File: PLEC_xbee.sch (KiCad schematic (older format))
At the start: 3 parts, among them IC1 XBP9B-DMST-002

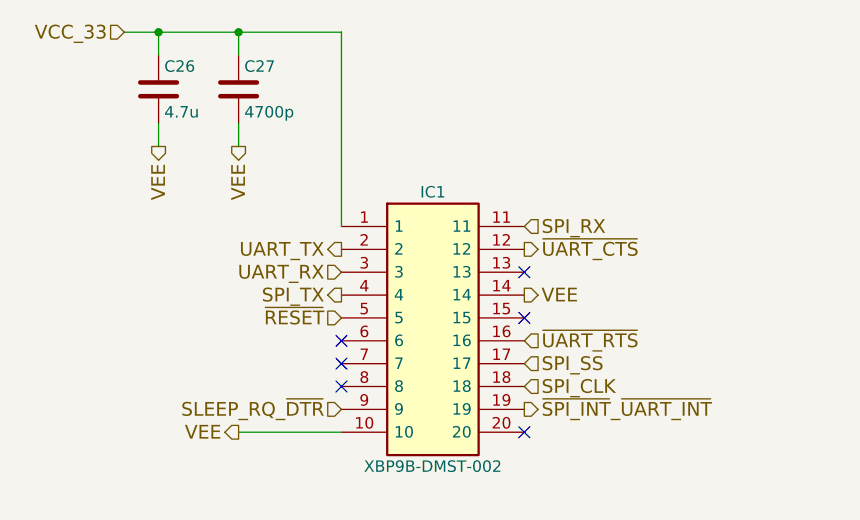
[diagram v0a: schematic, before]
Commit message: Almost done with layout; need to rearrange uC pins
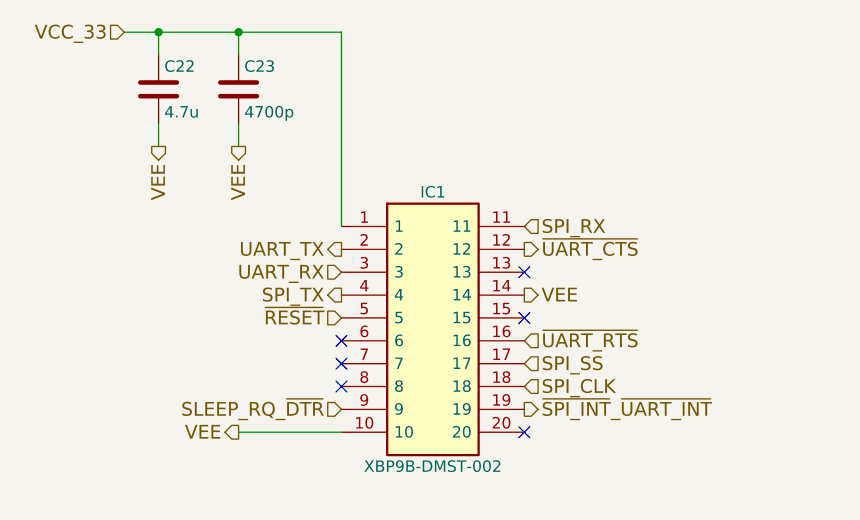
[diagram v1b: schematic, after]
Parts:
- renumbered C26 to C22, C27 to C23
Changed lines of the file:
@@
 NoConn ~ 4850 3800
 $Comp
-L C C27
+L C C23
 U 1 1 5A71C0C2
 P 4400 2500
-F 0 "C27" H 4425 2600 50  0000 L CNN
+F 0 "C23" H 4425 2600 50  0000 L CNN
 F 1 "4700p" H 4425 2400 50  0000 L CNN
 F 2 "PLEC:THTt_100Px150Lx100Wx183H_4700p" H 4438 2350 50  0001 C CNN
@@
 	4400 2750 4400 2650
 $Comp
-L C C26
+L C C22
 U 1 1 5A76736C
 P 4050 2500
-F 0 "C26" H 4075 2600 50  0000 L CNN
+F 0 "C22" H 4075 2600 50  0000 L CNN
 F 1 "4.7u" H 4075 2400 50  0000 L CNN
 F 2 "PLEC:THTm_1.5Px4Dx7H_4.7u" H 4088 2350 50  0001 C CNN

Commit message: Replaced solid state relays with NPN Darlingtons
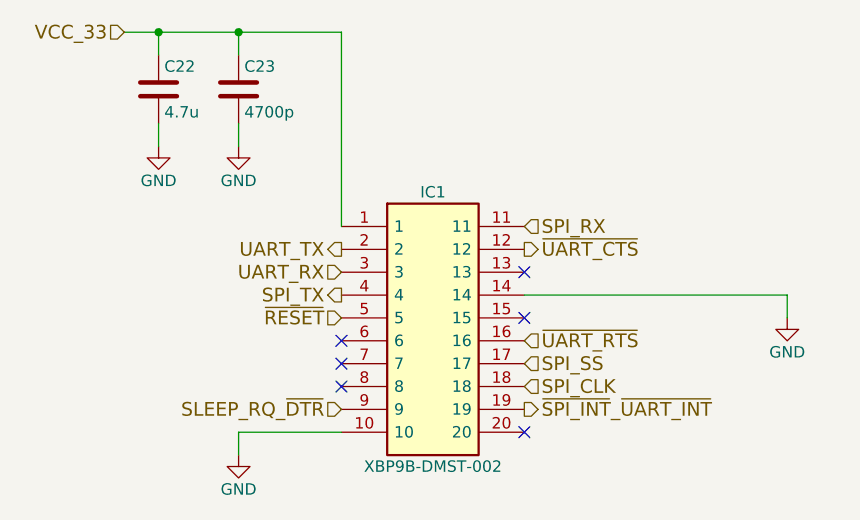
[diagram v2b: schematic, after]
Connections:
- net VEE renamed GND
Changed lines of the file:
@@
 EESchema Schematic File Version 2
+LIBS:PLEC-rescue
 LIBS:power
 LIBS:device
@@
 LIBS:PLEC
 LIBS:cap_470u
+LIBS:BDW42G
 LIBS:PLEC-cache
 EELAYER 25 0
@@
 $Descr A4 11693 8268
 encoding utf-8
-Sheet 7 9
+Sheet 6 9
 Title ""
 Date ""
@@
 NoConn ~ 4850 3700
 NoConn ~ 4850 3600
-Text HLabel 4400 4000 0    60   Output ~ 0
-VEE
-Text HLabel 5650 3400 2    60   Output ~ 0
-VEE
-Text HLabel 4400 2750 3    60   Output ~ 0
-VEE
 Wire Wire Line
 	4400 2350 4400 2250
@@
 	1    0    0    -1
 $EndComp
-Text HLabel 4050 2750 3    60   Output ~ 0
-VEE
 Wire Wire Line
 	4050 2750 4050 2650
@@
 	4050 2350 4050 2250
 Connection ~ 4050 2250
+Wire Wire Line
+	4400 4100 4400 4000
+$Comp
+L GND #PWR028
+U 1 1 5A8488B5
+P 4400 4100
+F 0 "#PWR028" H 4400 3850 50  0001 C CNN
+F 1 "GND" H 4400 3950 50  0000 C CNN
+F 2 "" H 4400 4100 50  0001 C CNN
+F 3 "" H 4400 4100 50  0001 C CNN
+	1    4400 4100
+	1    0    0    -1
+$EndComp
+Wire Wire Line
+	5650 3400 6800 3400
+Wire Wire Line
+	6800 3400 6800 3500
+$Comp
+L GND #PWR029
+U 1 1 5A848C7E
+P 6800 3500
+F 0 "#PWR029" H 6800 3250 50  0001 C CNN
+F 1 "GND" H 6800 3350 50  0000 C CNN
+F 2 "" H 6800 3500 50  0001 C CNN
+F 3 "" H 6800 3500 50  0001 C CNN
+	1    6800 3500
+	1    0    0    -1
+$EndComp
+$Comp
+L GND #PWR030
+U 1 1 5A8494C9
+P 4050 2750
+F 0 "#PWR030" H 4050 2500 50  0001 C CNN
+F 1 "GND" H 4050 2600 50  0000 C CNN
+F 2 "" H 4050 2750 50  0001 C CNN
+F 3 "" H 4050 2750 50  0001 C CNN
+	1    4050 2750
+	1    0    0    -1
+$EndComp
+$Comp
+L GND #PWR031
+U 1 1 5A8494DD
+P 4400 2750
+F 0 "#PWR031" H 4400 2500 50  0001 C CNN
+F 1 "GND" H 4400 2600 50  0000 C CNN
+F 2 "" H 4400 2750 50  0001 C CNN
+F 3 "" H 4400 2750 50  0001 C CNN
+	1    4400 2750
+	1    0    0    -1
+$EndComp
 $EndSCHEMATC
